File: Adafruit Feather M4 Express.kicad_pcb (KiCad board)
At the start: 2 copper layers, 50.8 x 22.9 mm, 109 parts, among them Q3 DMG341, SW1 KMR2, U1 2MB Flash, U2 AP2112-3.3, U3 MCP73831T-2ACI/OT, X1 JSTPH, X2 32.768, X3 microUSB

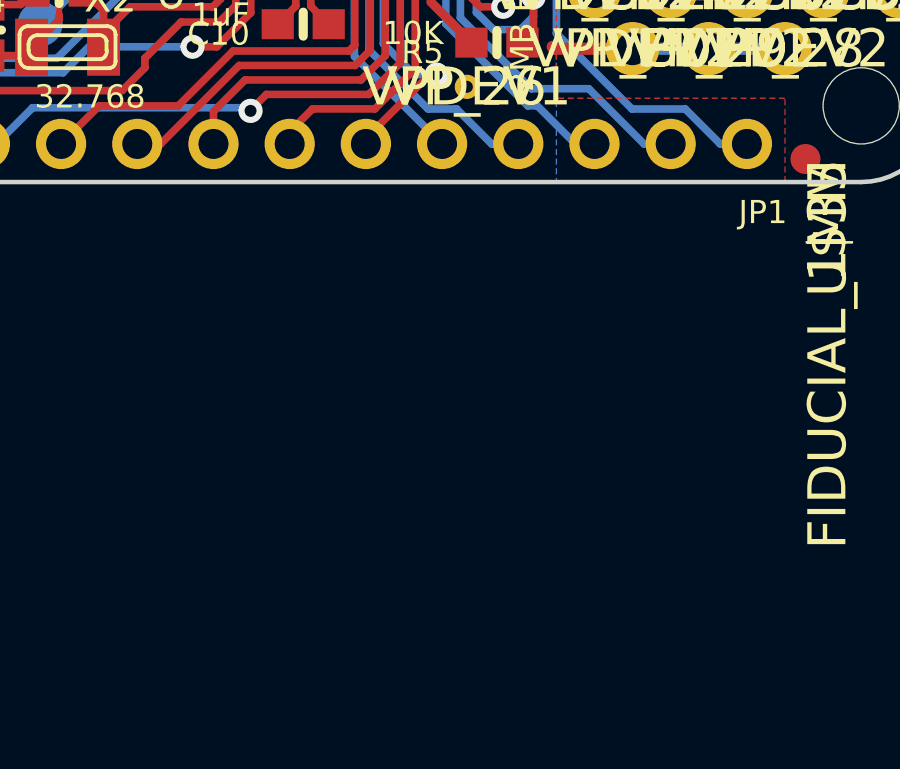
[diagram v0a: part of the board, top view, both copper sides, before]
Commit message: Major update to board and GND pads
Added the Grove connectors.
Had to edit settings for the GND pads so that they tied to the copper pour with 'solid' instead of 'spokes' so that the pour areas would connect more. Also had to redefine the USB connector pins so that they were on the GND net. I'm getting some DRC errors that I think are erroneous, but I don't know why...
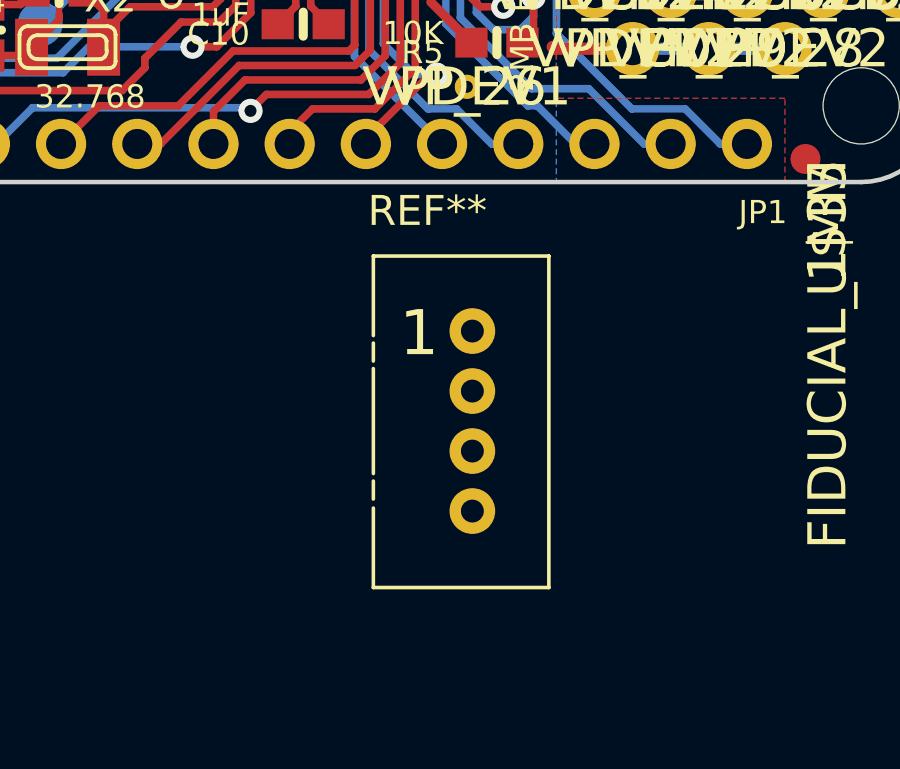
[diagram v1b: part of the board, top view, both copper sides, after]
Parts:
- added REF**: Grove_1x04, Connectors:Grove_1x04, F.Cu at (158.4, 121.4)
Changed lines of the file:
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@@
     (links 158)
     (no_connects 53)
-    (area 120.651386 91.74922 177.076529 135.06674)
+    (area 119.013448 91.74922 177.076529 135.06674)
     (thickness 1.6)
     (drawings 210)
     (tracks 596)
     (zones 0)
-    (modules 109)
+    (modules 110)
     (nets 75)
   )
@@
     (pad_to_mask_clearance 0.2)
     (aux_axis_origin 0 0)
-    (visible_elements FFFFFF7F)
+    (visible_elements FFFCFF7F)
     (pcbplotparams
       (layerselection 0x00030_80000001)
@@
       (net 74 N$32))
   )
+  (module Connectors:Grove_1x04 (layer Top)
+    (at 158.4 121.4)
+    (descr https://statics3.seeedstudio.com/images/opl/datasheet/3470130P1.pdf)
+    (tags Grove-1x04)
+    (fp_text reference REF** (at -1.5 -4) (layer F.SilkS)
+      (effects (font (size 1 1) (thickness 0.15)))
+    )
+    (fp_text value Grove_1x04 (at 4.19 2.83 90) (layer F.Fab)
+      (effects (font (size 1 1) (thickness 0.15)))
+    )
+    (fp_line (start -3.45 -2.65) (end -3.45 8.7) (layer F.CrtYd) (width 0.05))
+    (fp_line (start -3.45 8.7) (end 2.7 8.7) (layer F.CrtYd) (width 0.05))
+    (fp_line (start 2.7 8.7) (end 2.7 -2.65) (layer F.CrtYd) (width 0.05))
+    (fp_line (start -3.45 -2.65) (end 2.7 -2.65) (layer F.CrtYd) (width 0.05))
+    (fp_line (start -3.3 5) (end -3.3 5.6) (layer F.SilkS) (width 0.12))
+    (fp_line (start -3.3 0.4) (end -3.3 1) (layer F.SilkS) (width 0.12))
+    (fp_line (start 2.55 -2.5) (end 2.55 8.55) (layer F.SilkS) (width 0.12))
+    (fp_line (start -3.3 -2.5) (end 2.55 -2.5) (layer F.SilkS) (width 0.12))
+    (fp_line (start -3.3 1.25) (end -3.3 4.75) (layer F.SilkS) (width 0.12))
+    (fp_line (start -3.3 8.55) (end 2.55 8.55) (layer F.SilkS) (width 0.12))
+    (fp_line (start -3.3 -2.5) (end -3.3 0.15) (layer F.SilkS) (width 0.12))
+    (fp_line (start -3.3 5.9) (end -3.3 8.55) (layer F.SilkS) (width 0.12))
+    (fp_line (start -2.9 -2.1) (end 2.2 -2.1) (layer F.Fab) (width 0.1))
+    (fp_line (start 2.2 -2.1) (end 2.2 8.1) (layer F.Fab) (width 0.1))
+    (fp_line (start 2.2 8.1) (end -2.9 8.1) (layer F.Fab) (width 0.1))
+    (fp_line (start -2.9 8.1) (end -2.9 -2.1) (layer F.Fab) (width 0.1))
+    (fp_text user 1 (at -1.775 0.075) (layer F.SilkS)
+      (effects (font (size 1.5 1.5) (thickness 0.12)))
+    )
+    (pad 1 thru_hole circle (at 0 0) (size 1.524 1.524) (drill 0.762) (layers *.Cu *.Mask F.SilkS))
+    (pad 2 thru_hole circle (at 0 2) (size 1.524 1.524) (drill 0.762) (layers *.Cu *.Mask F.SilkS))
+    (pad 3 thru_hole circle (at 0 4) (size 1.524 1.524) (drill 0.762) (layers *.Cu *.Mask F.SilkS))
+    (pad 4 thru_hole circle (at 0 6) (size 1.524 1.524) (drill 0.762) (layers *.Cu *.Mask F.SilkS))
+    (model ${KISYS3DMOD}/Connectors.3dshapes/Grove_1x04.wrl
+      (at (xyz 0 0 0))
+      (scale (xyz 0.3937 0.3937 0.3937))
+      (rotate (xyz 0 0 -90))
+    )
+  )
   (gr_line (start 125.6411 116.4336) (end 171.3611 116.4336) (layer Edge.Cuts) (width 0.15))
